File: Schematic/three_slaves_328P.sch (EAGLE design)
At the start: 9 parts, among them IC1 ATMEGA328P

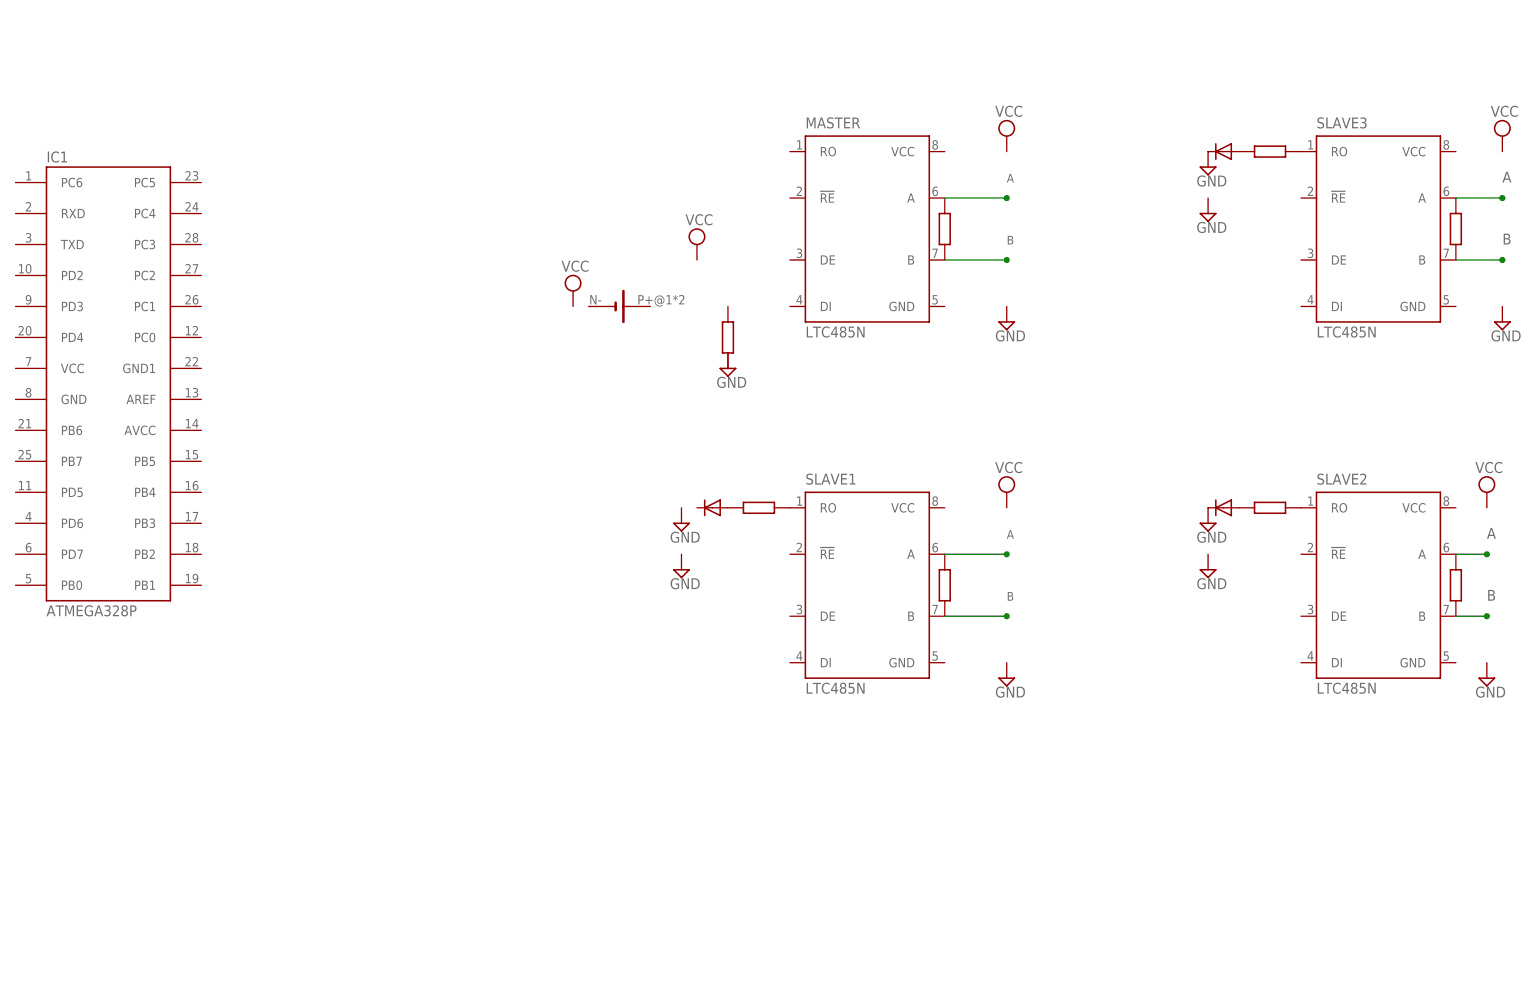
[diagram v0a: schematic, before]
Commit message: 328P and rs485 schematic
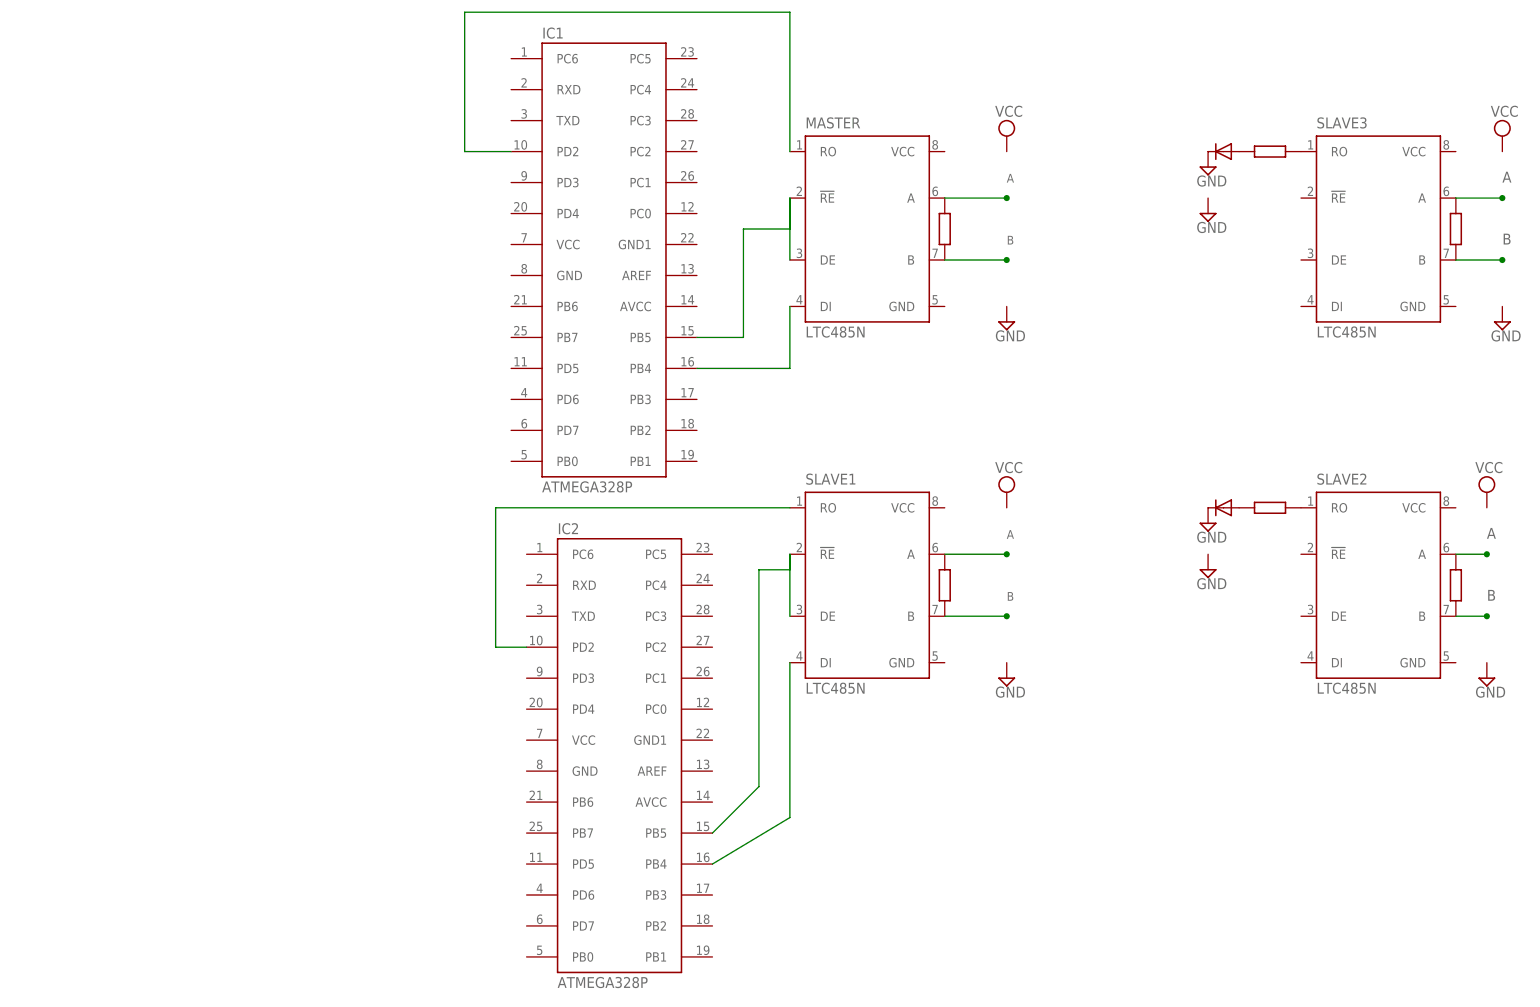
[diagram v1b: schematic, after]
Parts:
- removed D1: 1N4004, diode:1N4004
- removed G1: BATTERY-HOLDER_11.6MM, battery:BATTERY-HOLDER_11.6MM
- added IC2: ATMEGA328P, Arduino-AVR:ATMEGA328P
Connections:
- new net N$1: IC1.PB5, MASTER.!RE, MASTER.DE
- new net N$2: IC1.PB4, MASTER.DI
- new net N$3: IC1.PD2, MASTER.RO
- new net N$4: IC2.PB5, SLAVE1.!RE, SLAVE1.DE
- new net N$5: IC2.PB4, SLAVE1.DI
- new net N$6: IC2.PD2, SLAVE1.RO
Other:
- moved on the sheet: IC1
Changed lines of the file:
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@@
 <part name="SUPPLY3" library="supply2" deviceset="GND" device=""/>
 <part name="SUPPLY4" library="supply2" deviceset="VCC" device=""/>
-<part name="R3" library="docu-dummy" deviceset="R" device=""/>
-<part name="D1" library="diode" deviceset="1N4004" device=""/>
-<part name="SUPPLY5" library="supply2" deviceset="GND" device=""/>
-<part name="SUPPLY6" library="supply2" deviceset="GND" device=""/>
-<part name="SUPPLY7" library="supply2" deviceset="GND" device=""/>
-<part name="R4" library="docu-dummy" deviceset="R" device=""/>
-<part name="SUPPLY8" library="supply2" deviceset="VCC" device=""/>
-<part name="G1" library="battery" deviceset="BATTERY-HOLDER_11.6MM" device=""/>
-<part name="SUPPLY9" library="supply2" deviceset="VCC" device=""/>
 <part name="SLAVE2" library="linear-technology" deviceset="LTC485" device="N"/>
 <part name="SLAVE3" library="linear-technology" deviceset="LTC485" device="N"/>
@@
 <part name="R8" library="docu-dummy" deviceset="R" device=""/>
 <part name="IC1" library="Arduino-AVR" deviceset="ATMEGA328P" device=""/>
+<part name="IC2" library="Arduino-AVR" deviceset="ATMEGA328P" device=""/>
 </parts>
 <sheets>
@@
 <wire x1="0" y1="144.78" x2="10.16" y2="144.78" width="0.1524" layer="90"/>
 <wire x1="0" y1="119.38" x2="10.16" y2="119.38" width="0.1524" layer="90"/>
-<wire x1="-40.64" y1="86.36" x2="-43.18" y2="86.36" width="0.1524" layer="90"/>
-<wire x1="-25.4" y1="78.74" x2="-25.4" y2="60.96" width="0.1524" layer="90"/>
-<wire x1="-25.4" y1="78.74" x2="-43.18" y2="78.74" width="0.1524" layer="90"/>
-<wire x1="-25.4" y1="137.16" x2="-25.4" y2="127" width="0.1524" layer="90"/>
-<wire x1="-25.4" y1="127" x2="-40.64" y2="127" width="0.1524" layer="90"/>
-<wire x1="-25.4" y1="119.38" x2="-50.8" y2="119.38" width="0.1524" layer="90"/>
-<wire x1="-58.42" y1="119.38" x2="-60.96" y2="119.38" width="0.1524" layer="90"/>
 <wire x1="83.82" y1="86.36" x2="88.9" y2="86.36" width="0.1524" layer="90"/>
 <wire x1="83.82" y1="60.96" x2="88.9" y2="60.96" width="0.1524" layer="90"/>
@@
 <instance part="SUPPLY3" gate="GND" x="10.16" y="116.84"/>
 <instance part="SUPPLY4" gate="G$1" x="10.16" y="147.32"/>
-<instance part="R3" gate="G$1" x="-30.48" y="86.36"/>
-<instance part="D1" gate="1" x="-38.1" y="86.36" rot="R180"/>
-<instance part="SUPPLY5" gate="GND" x="-43.18" y="83.82"/>
-<instance part="SUPPLY6" gate="GND" x="-43.18" y="76.2"/>
-<instance part="SUPPLY7" gate="GND" x="-35.56" y="109.22"/>
-<instance part="R4" gate="G$1" x="-35.56" y="114.3" rot="R90"/>
-<instance part="SUPPLY8" gate="G$1" x="-40.64" y="129.54"/>
-<instance part="G1" gate="G$1" x="-53.34" y="119.38"/>
-<instance part="SUPPLY9" gate="G$1" x="-60.96" y="121.92"/>
 <instance part="SLAVE2" gate="G$1" x="71.12" y="76.2"/>
 <instance part="SLAVE3" gate="G$1" x="71.12" y="134.62"/>
@@
 <instance part="R7" gate="G$1" x="83.82" y="73.66" rot="R90"/>
 <instance part="R8" gate="G$1" x="83.82" y="132.08" rot="R90"/>
-<instance part="IC1" gate="1" x="-121.92" y="111.76"/>
+<instance part="IC1" gate="1" x="-40.64" y="132.08"/>
+<instance part="IC2" gate="1" x="-38.1" y="50.8"/>
 </instances>
 <busses>
@@
 </segment>
 </net>
+<net name="N$1" class="0">
+<segment>
+<pinref part="IC1" gate="1" pin="PB5"/>
+<wire x1="-40.64" y1="114.3" x2="-33.02" y2="114.3" width="0.1524" layer="91"/>
+<wire x1="-33.02" y1="114.3" x2="-33.02" y2="132.08" width="0.1524" layer="91"/>
+<wire x1="-33.02" y1="132.08" x2="-25.4" y2="132.08" width="0.1524" layer="91"/>
+<pinref part="MASTER" gate="G$1" pin="!RE"/>
+<wire x1="-25.4" y1="132.08" x2="-25.4" y2="137.16" width="0.1524" layer="91"/>
+<pinref part="MASTER" gate="G$1" pin="DE"/>
+<wire x1="-25.4" y1="137.16" x2="-25.4" y2="127" width="0.1524" layer="91"/>
+</segment>
+</net>
+<net name="N$2" class="0">
+<segment>
+<pinref part="IC1" gate="1" pin="PB4"/>
+<pinref part="MASTER" gate="G$1" pin="DI"/>
+<wire x1="-40.64" y1="109.22" x2="-25.4" y2="109.22" width="0.1524" layer="91"/>
+<wire x1="-25.4" y1="109.22" x2="-25.4" y2="119.38" width="0.1524" layer="91"/>
+</segment>
+</net>
+<net name="N$3" class="0">
+<segment>
+<pinref part="IC1" gate="1" pin="PD2"/>
+<wire x1="-71.12" y1="144.78" x2="-78.74" y2="144.78" width="0.1524" layer="91"/>
+<wire x1="-78.74" y1="144.78" x2="-78.74" y2="167.64" width="0.1524" layer="91"/>
+<pinref part="MASTER" gate="G$1" pin="RO"/>
+<wire x1="-78.74" y1="167.64" x2="-25.4" y2="167.64" width="0.1524" layer="91"/>
+<wire x1="-25.4" y1="167.64" x2="-25.4" y2="144.78" width="0.1524" layer="91"/>
+</segment>
+</net>
+<net name="N$4" class="0">
+<segment>
+<pinref part="IC2" gate="1" pin="PB5"/>
+<wire x1="-38.1" y1="33.02" x2="-30.48" y2="40.64" width="0.1524" layer="91"/>
+<wire x1="-30.48" y1="40.64" x2="-30.48" y2="76.2" width="0.1524" layer="91"/>
+<wire x1="-30.48" y1="76.2" x2="-25.4" y2="76.2" width="0.1524" layer="91"/>
+<pinref part="SLAVE1" gate="G$1" pin="!RE"/>
+<wire x1="-25.4" y1="76.2" x2="-25.4" y2="78.74" width="0.1524" layer="91"/>
+<pinref part="SLAVE1" gate="G$1" pin="DE"/>
+<wire x1="-25.4" y1="78.74" x2="-25.4" y2="68.58" width="0.1524" layer="91"/>
+</segment>
+</net>
+<net name="N$5" class="0">
+<segment>
+<pinref part="SLAVE1" gate="G$1" pin="DI"/>
+<wire x1="-25.4" y1="60.96" x2="-25.4" y2="35.56" width="0.1524" layer="91"/>
+<pinref part="IC2" gate="1" pin="PB4"/>
+<wire x1="-25.4" y1="35.56" x2="-38.1" y2="27.94" width="0.1524" layer="91"/>
+</segment>
+</net>
+<net name="N$6" class="0">
+<segment>
+<pinref part="IC2" gate="1" pin="PD2"/>
+<wire x1="-68.58" y1="63.5" x2="-73.66" y2="63.5" width="0.1524" layer="91"/>
+<wire x1="-73.66" y1="63.5" x2="-73.66" y2="86.36" width="0.1524" layer="91"/>
+<pinref part="SLAVE1" gate="G$1" pin="RO"/>
+<wire x1="-73.66" y1="86.36" x2="-25.4" y2="86.36" width="0.1524" layer="91"/>
+</segment>
+</net>
